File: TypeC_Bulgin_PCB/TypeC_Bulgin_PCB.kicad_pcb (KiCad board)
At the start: 2 copper layers, 16.1 x 16.1 mm, 4 parts, among them J1 Conn_01x01_Female, J3 Conn_01x13, J4 Conn_01x13, J6 USB_C_Receptacle

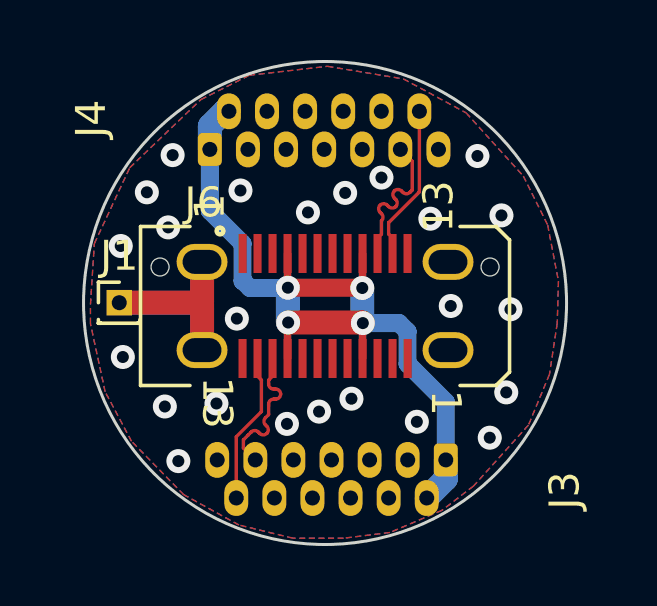
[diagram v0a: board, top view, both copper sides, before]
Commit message: v0.2 TXn were swapped
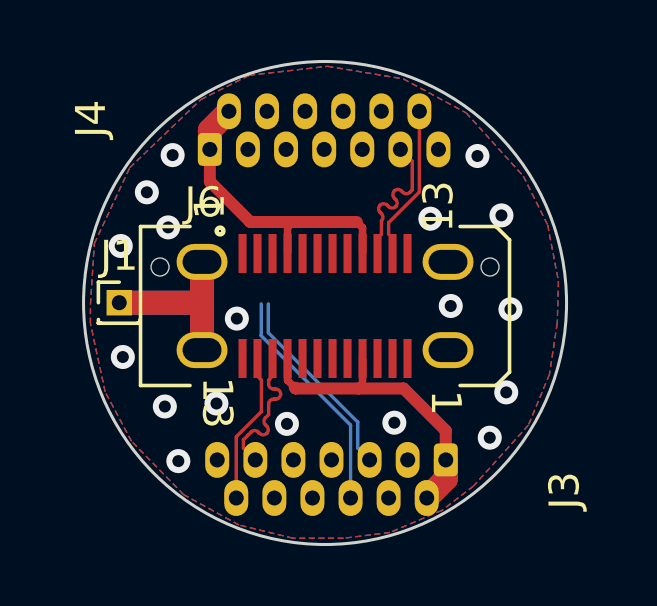
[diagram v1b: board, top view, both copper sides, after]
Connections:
- J6 pad A2: TX1+ -> TX1-
- J6 pad A3: TX1- -> TX1+
- J6 pad B2: TX2+ -> TX2-
- J6 pad B3: TX2- -> TX2+
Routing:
- net TX1-: track 0.00 -> 7.70 mm
- net VBUS: track 28.1 -> 20.6 mm, vias 4 -> 0
- net TX1+: track 0.00 -> 6.60 mm
- net GND: vias 24 -> 18

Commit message: v0.3 Seems 2B ready
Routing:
- net TX2-: track 0.00 -> 9.73 mm, vias 0 -> 1
- net TX2+: track 0.00 -> 9.68 mm, vias 0 -> 1
- net TX1+: track 6.60 -> 9.67 mm, vias 0 -> 1
- net TX1-: track 7.70 -> 9.72 mm, vias 0 -> 1
- net GND: vias 18 -> 20

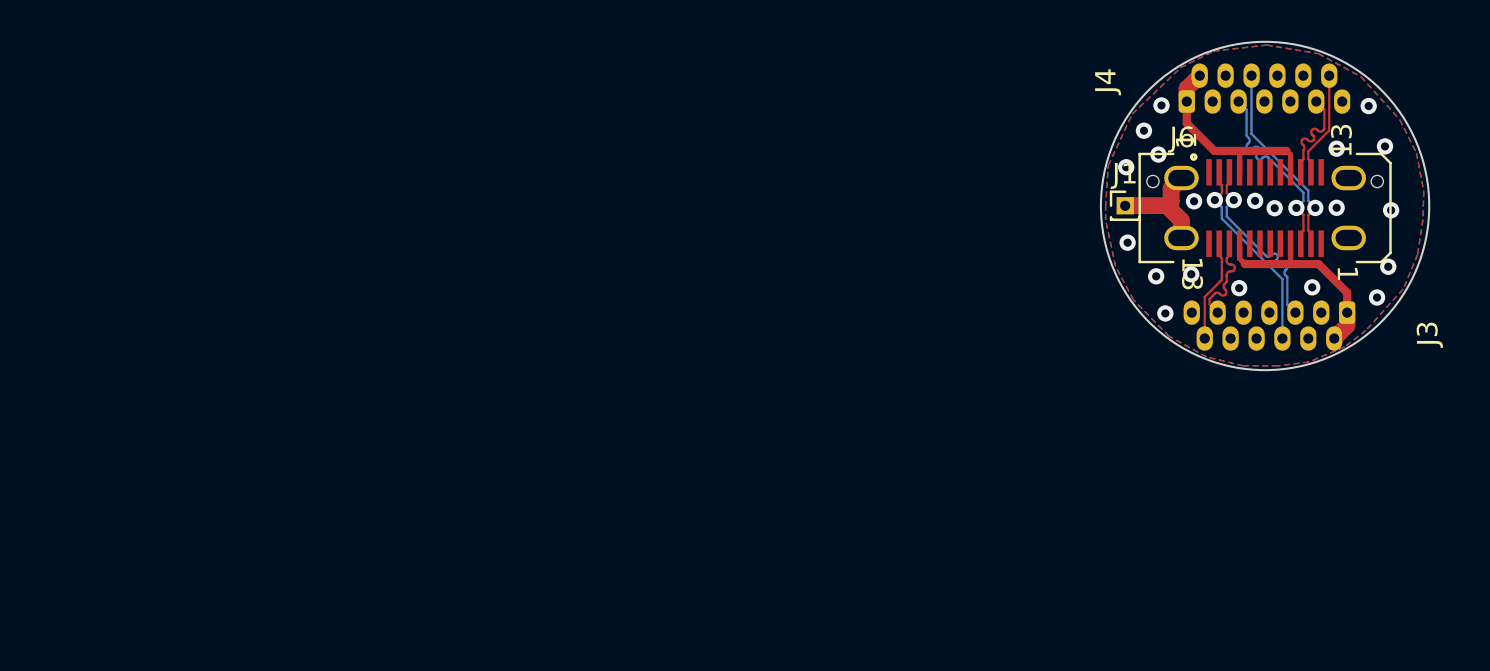
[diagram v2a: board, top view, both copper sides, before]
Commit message: v0.4 key & axes were added
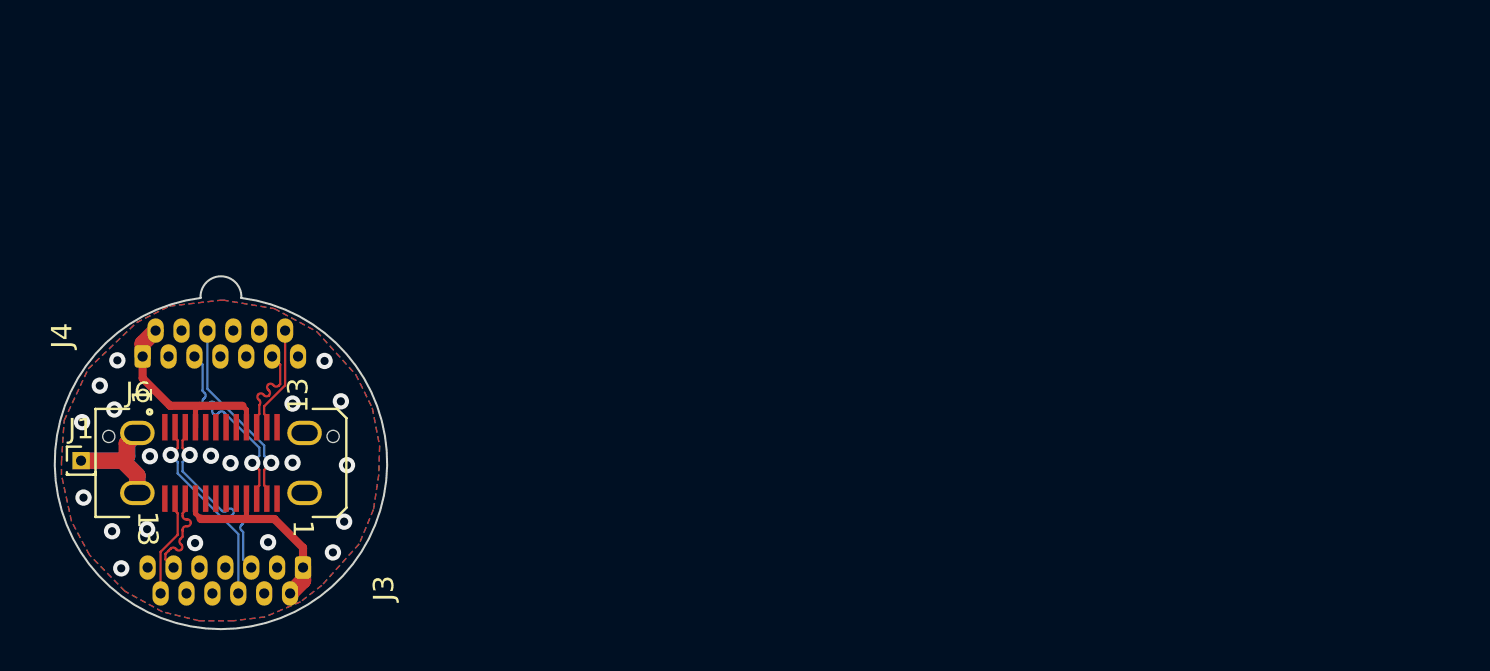
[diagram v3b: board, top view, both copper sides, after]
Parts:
- moved J4 52.7 mm to (96.2, 94.8)
- moved J1 52.7 mm to (93.1, 99.9)
- moved J3 52.7 mm to (104.0, 105.1)
- moved J6 52.7 mm to (100.0, 100.0)
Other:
- board size 16.1 x 16.1 mm -> 16.3 x 17.3 mm
